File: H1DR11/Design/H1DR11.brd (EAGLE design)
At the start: 34.6 x 30 mm, 34 parts, among them P1 HEXABIT_17.32_NO_P6, P2 RS-485, U1 STM32F091CBU6, U2 MAX14840EASAT, X1 XTALL_CSTCE8M00G52

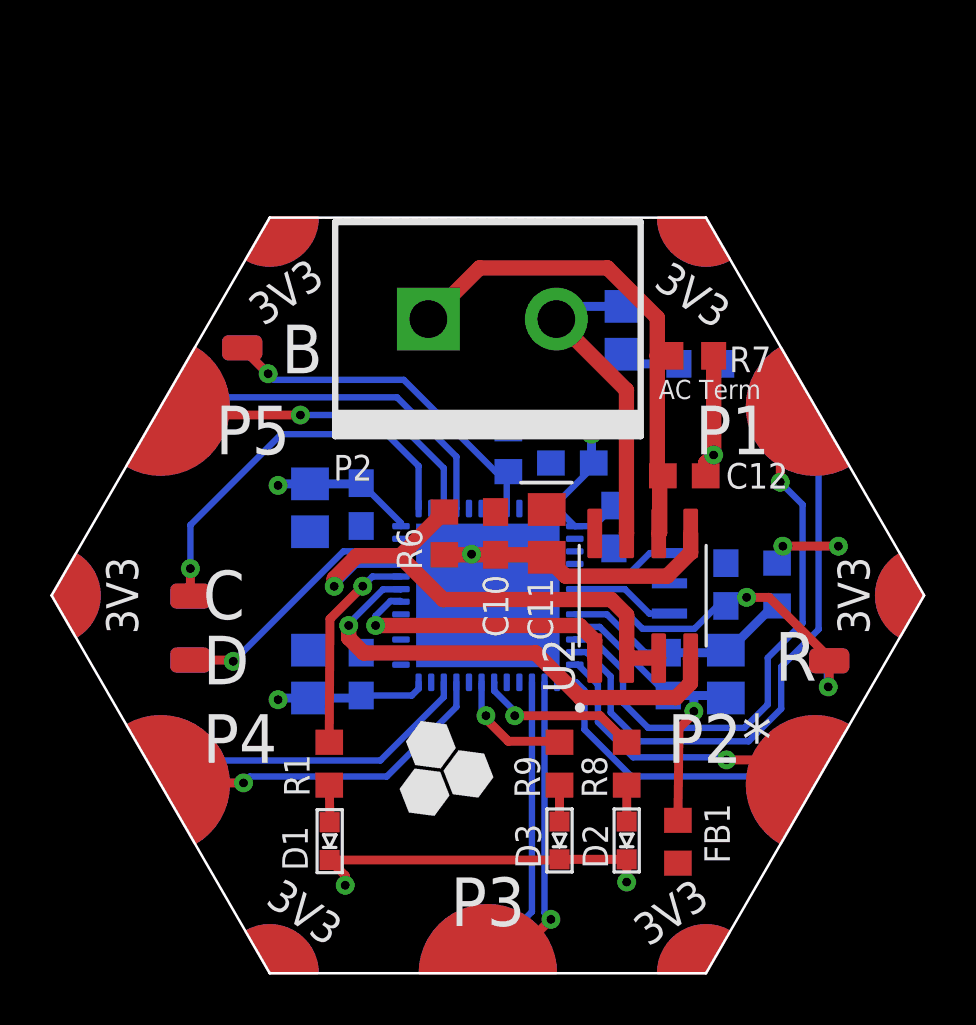
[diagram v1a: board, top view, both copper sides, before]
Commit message: fix  connector problems
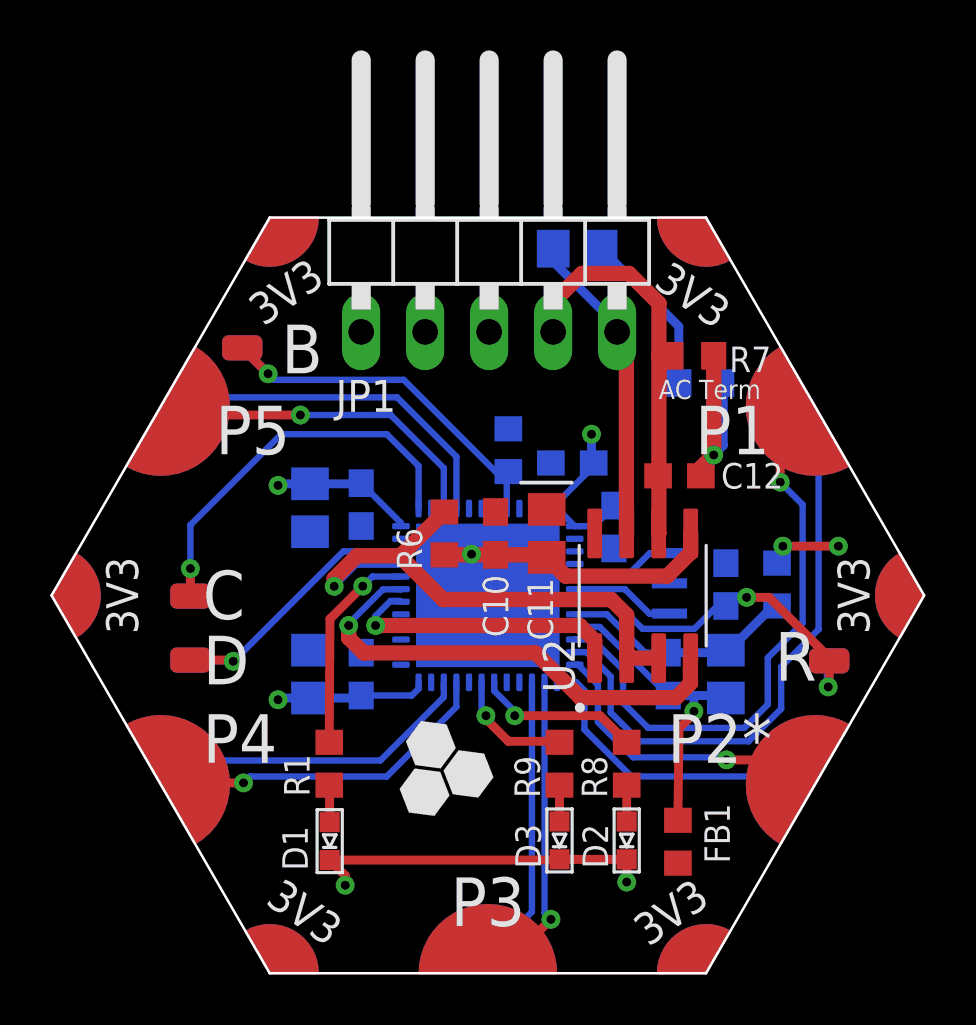
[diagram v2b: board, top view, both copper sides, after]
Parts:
- removed P2: RS-485, Hexabitz:1546111-2
- added JP1: (no value), Hexabitz:1X05/90
- moved R5 3.73 mm to (38.2, 48.4), turned to 180 degrees
- moved R4 0.76 mm to (43.1, 43.1)
- moved C12 0.19 mm to (42.2, 39.4)
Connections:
- net GND: now also JP1.1
- net TA: now also JP1.4; no longer P2.1
- net TB: now also JP1.5; no longer P2.2
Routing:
- net N$10: track 2.36 -> 6.61 mm
- net TA: track 20.6 -> 16.5 mm
- net N$2: track 8.65 -> 8.01 mm
